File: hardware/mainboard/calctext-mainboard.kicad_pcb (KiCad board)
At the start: 4 copper layers, 65 x 97.8 mm, 85 parts, among them J1 LCD_FFC, J2 J_BAT+, J3 J_BAT-, SW1 Keypad_Contact, U1 Wio-E5-LE, U2 TPS61299, U3 PCAL9535APW,118

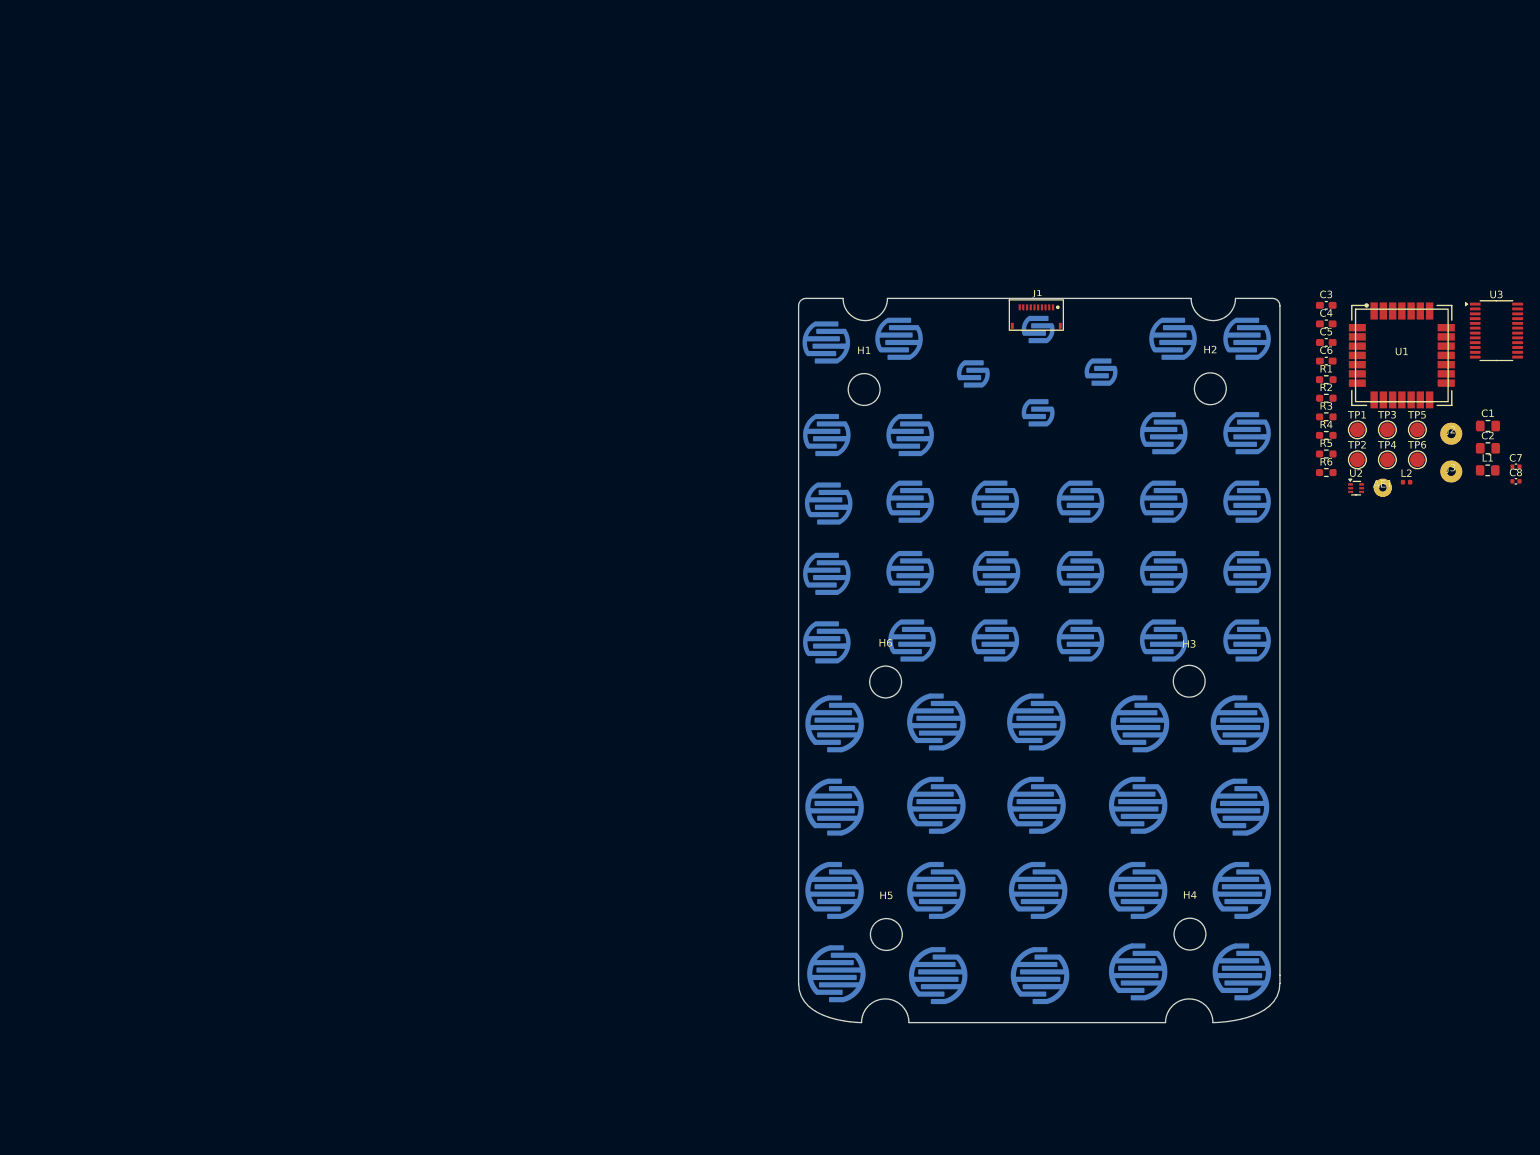
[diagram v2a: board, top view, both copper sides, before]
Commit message: Complete mainboard PCB layout
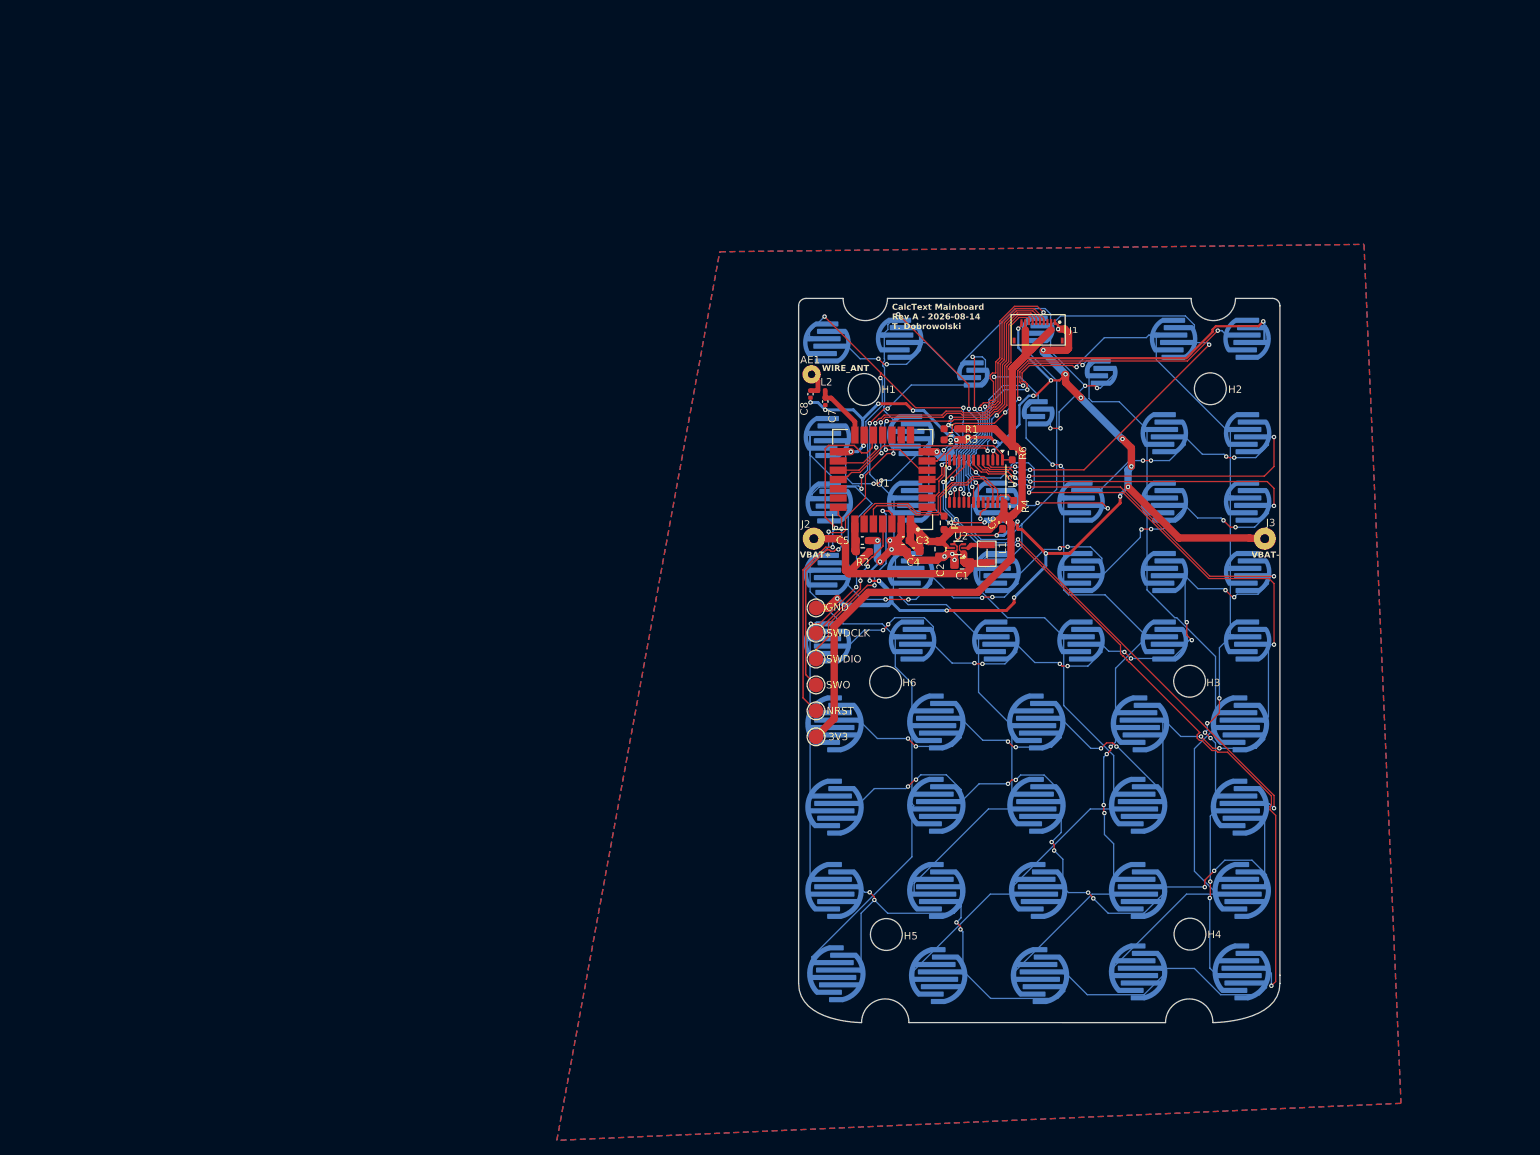
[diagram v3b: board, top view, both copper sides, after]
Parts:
- L1: footprint Inductor_SMD:L_0805_2012Metric_Pad1.15x1.40mm_HandSolder -> CalcText:L_INPAQ_WIP252010
- SW10, SW11, SW12, SW17, SW18, SW19, SW2, SW24, SW25, SW26, SW3, SW31, SW32, SW33, SW38, SW39, SW4, SW40, SW44, SW45, SW46, SW47, SW48, SW5, SW9: renamed from REF**; value keypad_trace_button_medium -> Keypad_Contact
- SW13, SW14, SW15, SW20, SW21, SW22, SW27, SW28, SW29, SW34, SW35, SW36, SW41, SW42, SW43, SW49, SW50, SW6, SW7, SW8: renamed from REF**; value keypad_trace_button_large -> Keypad_Contact
- SW16, SW23, SW30, SW37: renamed from REF**; value keypad_trace_button_small -> Keypad_Contact
- moved C8 96.0 mm to (120.2, 65.2), turned to -90 degrees
- moved C7 93.7 mm to (122.2, 66.2), turned to -90 degrees
- moved TP5 91.2 mm to (121.0, 111.5)
- moved J2 87.2 mm to (120.7, 84.8)
- moved TP3 86.0 mm to (121.0, 108.0)
- moved TP6 83.6 mm to (121.0, 94.1)
- moved TP4 82.9 mm to (121.0, 104.5)
- moved L2 80.0 mm to (121.7, 64.8), turned to 180 degrees
- moved TP1 79.4 mm to (121.0, 101.0)
- moved AE1 78.7 mm to (120.4, 62.5)
- moved TP2 76.8 mm to (121.0, 97.5)
- moved C2 75.2 mm to (137.8, 86.2), turned to -90 degrees
- moved C1 73.4 mm to (140.7, 88.1), turned to 180 degrees
- moved U3 73.2 mm to (142.6, 77.0), turned to -90 degrees
- moved U1 72.1 mm to (130.0, 76.8), turned to 180 degrees
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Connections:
- SW10 pad 1: (no net) -> COL2
- SW10 pad 2: (no net) -> ROW2
- SW11 pad 1: (no net) -> COL2
- SW11 pad 2: (no net) -> ROW3
- SW12 pad 1: (no net) -> COL2
- SW12 pad 2: (no net) -> ROW4
- SW13 pad 1: (no net) -> COL2
- SW13 pad 2: (no net) -> ROW5
- SW14 pad 1: (no net) -> COL2
- SW14 pad 2: (no net) -> ROW6
- SW15 pad 1: (no net) -> COL2
- SW15 pad 2: (no net) -> ROW7
- SW16 pad 1: (no net) -> COL3
- SW16 pad 2: (no net) -> ROW1
- SW17 pad 1: (no net) -> COL3
- SW17 pad 2: (no net) -> ROW2
- SW18 pad 1: (no net) -> COL3
- SW18 pad 2: (no net) -> ROW3
- SW19 pad 1: (no net) -> COL3
- SW19 pad 2: (no net) -> ROW4
- SW2 pad 1: (no net) -> COL1
- SW2 pad 2: (no net) -> ROW1
- SW20 pad 1: (no net) -> COL3
- SW20 pad 2: (no net) -> ROW5
- SW21 pad 1: (no net) -> COL3
- SW21 pad 2: (no net) -> ROW6
- SW22 pad 1: (no net) -> COL3
- SW22 pad 2: (no net) -> ROW7
- SW23 pad 1: (no net) -> COL4
- SW23 pad 2: (no net) -> ROW1
- SW24 pad 1: (no net) -> COL4
- SW24 pad 2: (no net) -> ROW2
- SW25 pad 1: (no net) -> COL4
- SW25 pad 2: (no net) -> ROW3
- SW26 pad 1: (no net) -> COL4
- SW26 pad 2: (no net) -> ROW4
- SW27 pad 1: (no net) -> COL4
- SW27 pad 2: (no net) -> ROW5
- SW28 pad 1: (no net) -> COL4
- SW28 pad 2: (no net) -> ROW6
- SW29 pad 1: (no net) -> COL4
- SW29 pad 2: (no net) -> ROW7
- SW3 pad 1: (no net) -> COL1
- SW3 pad 2: (no net) -> ROW2
- SW30 pad 1: (no net) -> COL5
- SW30 pad 2: (no net) -> ROW1
- SW31 pad 1: (no net) -> COL5
- SW31 pad 2: (no net) -> ROW2
- SW32 pad 1: (no net) -> COL5
- SW32 pad 2: (no net) -> ROW3
- SW33 pad 1: (no net) -> COL5
- SW33 pad 2: (no net) -> ROW4
- SW34 pad 1: (no net) -> COL5
- SW34 pad 2: (no net) -> ROW5
- SW35 pad 1: (no net) -> COL5
- SW35 pad 2: (no net) -> ROW6
- SW36 pad 1: (no net) -> COL5
- SW36 pad 2: (no net) -> ROW7
- SW37 pad 1: (no net) -> COL6
- SW37 pad 2: (no net) -> ROW1
- SW38 pad 1: (no net) -> COL6
- SW38 pad 2: (no net) -> ROW2
- SW39 pad 1: (no net) -> COL6
- SW39 pad 2: (no net) -> ROW3
- SW4 pad 1: (no net) -> COL1
- SW4 pad 2: (no net) -> ROW3
- SW40 pad 1: (no net) -> COL6
- SW40 pad 2: (no net) -> ROW4
- SW41 pad 1: (no net) -> COL6
- SW41 pad 2: (no net) -> ROW5
- SW42 pad 1: (no net) -> COL6
- SW42 pad 2: (no net) -> ROW6
- SW43 pad 1: (no net) -> COL6
- SW43 pad 2: (no net) -> ROW7
- SW44 pad 1: (no net) -> COL7
- SW44 pad 2: (no net) -> ROW1
- SW45 pad 1: (no net) -> COL7
- SW45 pad 2: (no net) -> ROW2
- SW46 pad 1: (no net) -> COL7
- SW46 pad 2: (no net) -> ROW3
- SW47 pad 1: (no net) -> COL7
- SW47 pad 2: (no net) -> ROW4
- SW48 pad 1: (no net) -> COL7
- SW48 pad 2: (no net) -> ROW5
- SW49 pad 1: (no net) -> COL7
- SW49 pad 2: (no net) -> ROW6
- SW5 pad 1: (no net) -> COL1
- SW5 pad 2: (no net) -> ROW4
- SW50 pad 1: (no net) -> COL7
- SW50 pad 2: (no net) -> ROW7
- SW6 pad 1: (no net) -> COL1
- SW6 pad 2: (no net) -> ROW5
- SW7 pad 1: (no net) -> COL1
- SW7 pad 2: (no net) -> ROW6
- SW8 pad 1: (no net) -> COL1
- SW8 pad 2: (no net) -> ROW7
- SW9 pad 1: (no net) -> COL2
- SW9 pad 2: (no net) -> ROW1
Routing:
- net GND: track 0.00 -> 238.5 mm, vias 0 -> 39
- net ROW7: track 0.00 -> 192.7 mm, vias 0 -> 7
- net COL4: track 0.00 -> 173.7 mm, vias 0 -> 3
- net ROW6: track 0.00 -> 166.3 mm, vias 0 -> 13
- net 3V3: track 0.00 -> 164.0 mm, vias 0 -> 1
- net ROW5: track 0.00 -> 159.8 mm, vias 0 -> 11
- net COL1: track 0.00 -> 146.0 mm, vias 0 -> 8
- net COL2: track 0.00 -> 143.8 mm, vias 0 -> 5
- net COL6: track 0.00 -> 138.7 mm, vias 0 -> 3
- net COL7: track 0.00 -> 137.9 mm, vias 0 -> 9
- net ROW2: track 0.00 -> 133.5 mm, vias 0 -> 13
- net ROW3: track 0.00 -> 130.7 mm, vias 0 -> 13
- net ROW4: track 0.00 -> 130.3 mm, vias 0 -> 15
- net ROW1: track 0.00 -> 128.9 mm, vias 0 -> 9
- net COL5: track 0.00 -> 126.6 mm, vias 0 -> 9
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- added copper zone on B.Cu, net GND
- added copper zone on F.Cu, net GND
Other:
- board text added: "CalcText Mainboard Rev A - 2026-08-14 T. Dobrowolski"
- board text added: "VBAT+"
- board text added: "VBAT-"
- board text added: "WIRE_ANT"
- board text removed: "H3"

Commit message: Refine hardware for fabrication and procurement
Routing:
- net GND: track 238.5 -> 238.3 mm, vias 39 -> 38
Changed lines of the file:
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@@
 		)
 		(pad_to_mask_clearance 0)
-		(solder_mask_min_width 0.12)
 		(allow_soldermask_bridges_in_footprints no)
 		(tenting front back)
 		(pcbplotparams
-			(layerselection 0x00000000_00000000_55555555_57555500)
+			(layerselection 0x00000000_00000000_55555555_575555af)
 			(plot_on_all_layers_selection 0x00000000_00000000_00000000_00000000)
 			(disableapertmacros no)
@@
 			(plotpadnumbers no)
 			(hidednponfab no)
-			(sketchdnponfab yes)
-			(crossoutdnponfab yes)
+			(sketchdnponfab no)
+			(crossoutdnponfab no)
 			(subtractmaskfromsilk yes)
-			(outputformat 3)
+			(outputformat 1)
 			(mirror no)
-			(drillshape 1)
+			(drillshape 0)
 			(scaleselection 1)
-			(outputdirectory "dxf/")
+			(outputdirectory "gerbers/")
 		)
 	)
@@
 		)
 	)
+	(dimension
+		(type orthogonal)
+		(layer "Cmts.User")
+		(pts
+			(xy 118.65 59.95) (xy 183.65 61.5)
+		)
+		(height -21.25)
+		(orientation 0)
+		(format
+			(prefix "")
+			(suffix "")
+			(units 3)
+			(units_format 0)
+			(precision 4)
+			(suppress_zeroes yes)
+		)
+		(style
+			(thickness 0.1)
+			(arrow_length 1.27)
+			(text_position_mode 0)
+			(arrow_direction outward)
+			(extension_height 0.58642)
+			(extension_offset 0.5)
+			(keep_text_aligned yes)
+		)
+		(gr_text "65"
+			(at 151.15 37.55 0)
+			(layer "Cmts.User")
+			(effects
+				(font
+					(size 1 1)
+					(thickness 0.15)
+				)
+			)
+		)
+	)
+	(dimension
+		(type orthogonal)
+		(layer "Cmts.User")
+		(pts
+			(xy 137.75 52.3) (xy 137.8 150.1)
+		)
+		(height -41)
+		(orientation 1)
+		(format
+			(prefix "")
+			(suffix "")
+			(units 3)
+			(units_format 0)
+			(precision 4)
+			(suppress_zeroes yes)
+		)
+		(style
+			(thickness 0.1)
+			(arrow_length 1.27)
+			(text_position_mode 0)
+			(arrow_direction outward)
+			(extension_height 0.58642)
+			(extension_offset 0.5)
+			(keep_text_aligned yes)
+		)
+		(gr_text "97.8"
+			(at 95.6 101.2 90)
+			(layer "Cmts.User")
+			(effects
+				(font
+					(size 1 1)
+					(thickness 0.15)
+				)
+			)
+		)
+	)
 	(segment
 		(start 121.25 64.75)
@@
 	)
 	(segment
-		(start 145.4 84.225002)
-		(end 146.2 83.425002)
-		(width 0.2)
-		(layer "F.Cu")
-		(net 3)
-	)
-	(segment
-		(start 145.4 84.3)
-		(end 140.660001 84.3)
-		(width 0.2)
-		(layer "F.Cu")
-		(net 3)
-	)
-	(segment
 		(start 139.4 86.801)
 		(end 139.46 86.801)
@@
 	)
 	(segment
+		(start 146.2 83.425002)
+		(end 145.174002 84.451)
+		(width 0.6)
+		(layer "F.Cu")
+		(net 3)
+	)
+	(segment
 		(start 133.274998 86.5)
 		(end 131.5 86.5)
@@
 	)
 	(segment
-		(start 140.660001 84.3)
-		(end 139.46 85.500001)
-		(width 0.2)
-		(layer "F.Cu")
-		(net 3)
-	)
-	(segment
 		(start 139 75.2)
 		(end 139 74.150001)
@@
 	)
 	(segment
-		(start 145.4 84.3)
-		(end 145.4 84.225002)
-		(width 0.2)
-		(layer "F.Cu")
-		(net 3)
-	)
-	(segment
 		(start 120.25 65.71)
 		(end 120.25 66.35)
@@
 	)
 	(segment
+		(start 145.174002 84.451)
+		(end 140.509001 84.451)
+		(width 0.6)
+		(layer "F.Cu")
+		(net 3)
+	)
+	(segment
 		(start 153.876023 63.371232)
 		(end 154.7 62.547255)
@@
 	)
 	(segment
+		(start 140.509001 84.451)
+		(end 139.561001 85.399)
+		(width 0.6)
+		(layer "F.Cu")
+		(net 3)
+	)
+	(segment
 		(start 150.655 65.445)
 		(end 152.728768 63.371232)
@@
 		(size 0.6)
 		(drill 0.3)
-		(layers "F.Cu" "B.Cu")
-		(net 3)
-	)
-	(via
-		(at 145.4 84.3)
-		(size 0.6)
-		(drill 0.3)

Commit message: Finalise hardware sanity-check cleanup
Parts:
- J1: value LCD_FFC -> FH34SRJ-10S-0.5SH
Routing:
- net ROW7: track 192.7 -> 193.6 mm
